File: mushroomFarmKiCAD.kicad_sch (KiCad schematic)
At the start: 10 parts

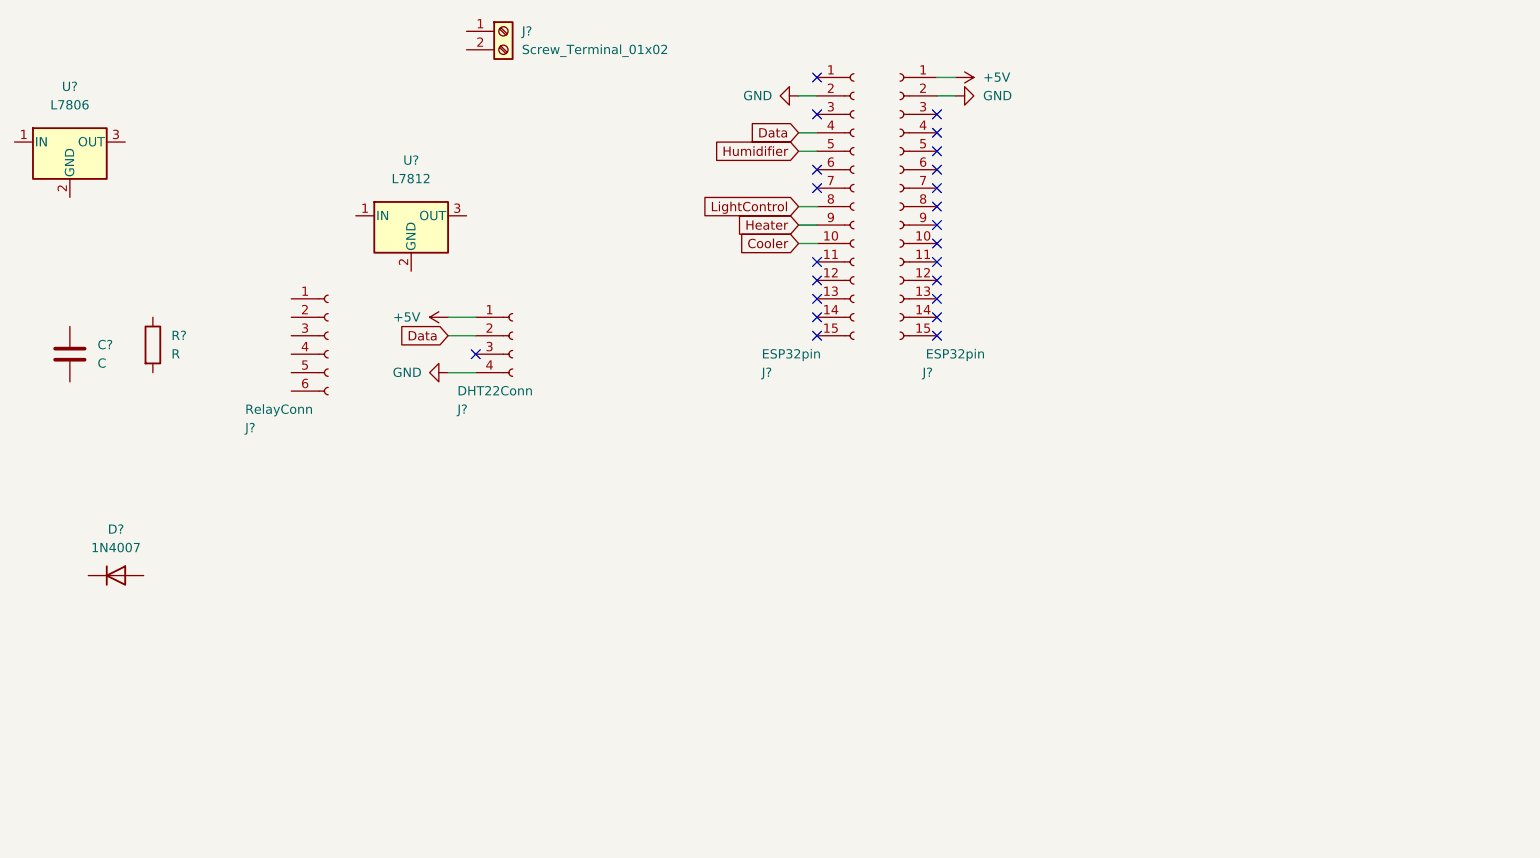
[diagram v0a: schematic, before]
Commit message: design circuit with wire and finalize schematic
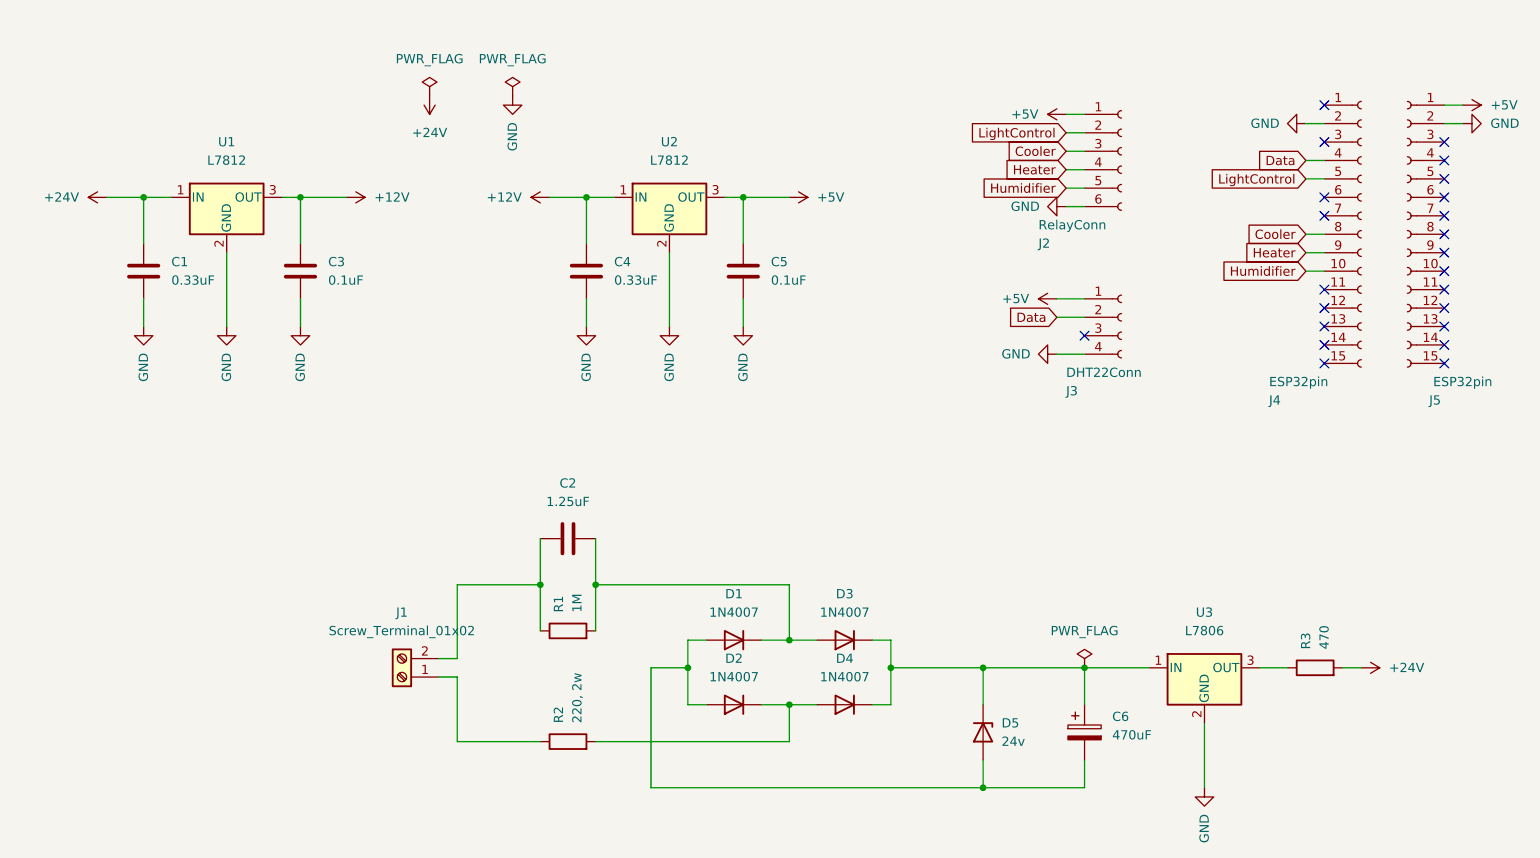
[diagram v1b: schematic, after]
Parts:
- added C2: 1.25uF, Capacitor_THT:C_Disc_D16.0mm_W5.0mm_P10.00mm, symbol Device:C
- added C3, C5: 0.1uF, Capacitor_THT:CP_Radial_D10.0mm_P5.00mm, symbol Device:C
- added C4: 0.33uF, Capacitor_THT:CP_Radial_D10.0mm_P5.00mm, symbol Device:C
- added C6: 470uF, Capacitor_THT:CP_Radial_D10.0mm_P5.00mm, symbol Device:C_Polarized
- added D1, D3, D4: 1N4007, Diode_THT:D_DO-41_SOD81_P10.16mm_Horizontal, symbol Diode:1N4007
- added D5: 24v, Diode_THT:D_DO-41_SOD81_P10.16mm_Horizontal, symbol Device:D_Zener
- added R2: 220, 2w, Resistor_THT:R_Axial_DIN0411_L9.9mm_D3.6mm_P12.70mm_Horizontal, symbol Device:R
- added R3: 470, Resistor_THT:R_Axial_DIN0411_L9.9mm_D3.6mm_P12.70mm_Horizontal, symbol Device:R
- added U2: L7812, Package_TO_SOT_THT:TO-262-3_Vertical, symbol Regulator_Linear:L7812
- C1: renamed from C?; value C -> 0.33uF; footprint (none) -> Capacitor_THT:CP_Radial_D8.0mm_P3.80mm
- J1: renamed from J?; footprint (none) -> TerminalBlock_Altech:Altech_AK300_1x02_P5.00mm_45-Degree
- J2: renamed from J?; footprint (none) -> Connector_PinHeader_2.54mm:PinHeader_1x06_P2.54mm_Vertical
- J3: renamed from J?; footprint (none) -> Connector_PinHeader_2.54mm:PinHeader_1x04_P2.54mm_Vertical
- J4: renamed from J?; footprint Connector_PinHeader_1.00mm:PinHeader_1x15_P1.00mm_Vertical -> Connector_PinHeader_2.54mm:PinHeader_1x15_P2.54mm_Vertical
- J5: renamed from J?; footprint (none) -> Connector_PinHeader_2.54mm:PinHeader_1x15_P2.54mm_Vertical
- R1: renamed from R?; value R -> 1M; footprint (none) -> Resistor_THT:R_Axial_DIN0411_L9.9mm_D3.6mm_P12.70mm_Horizontal
- U1, U3: renamed from U?; footprint (none) -> Package_TO_SOT_THT:TO-262-3_Vertical
- gave numbers to parts that had none: 1
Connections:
- net +5V: now also J2.1 (Pin_1), C5.1, U2.3 (OUT)
- net Cooler: now also J2.3 (Pin_3), J4.8 (Pin_8); no longer J4.10 (Pin_10)
- net GND: now also C1.2, J2.6 (Pin_6), U1.2 (GND), U3.2 (GND), C3.2, C4.2, C5.2, U2.2 (GND)
- net Heater: now also J2.4 (Pin_4)
- net Humidifier: now also J2.5 (Pin_5), J4.10 (Pin_10); no longer J4.5 (Pin_5)
- net LightControl: now also J2.2 (Pin_2), J4.5 (Pin_5); no longer J4.8 (Pin_8)
- net at J1.1 (Pin_1): now also R2.1
- net at J1.2 (Pin_2): now also R1.1, C2.1
- net at D2.1 (K): now also D4.2 (A), R2.2
- net at D2.2 (A): now also C6.2, D1.2 (A), D5.2 (A)
- net at U3.1 (IN): now also C6.1, D3.1 (K), D4.1 (K), D5.1 (K)
- net at U3.3 (OUT): now also R3.1
- net +24V: now reaches C1.1
- net +24V: now also U1.1 (IN), R3.2
- net +12V: now reaches U1.3 (OUT)
- net +12V: now also C3.1, C4.1, U2.1 (IN)
- net at R1.2: now also C2.2, D1.1 (K), D3.2 (A)
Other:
- moved on the sheet: C1, D2, J1, J2, J3, J4, J5, R1, U1, U3

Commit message: Created PCB added 3d models, improve pcb
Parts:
- J1: footprint TerminalBlock_Altech:Altech_AK300_1x02_P5.00mm_45-Degree -> TerminalBlock_Phoenix:TerminalBlock_Phoenix_MKDS-1,5-2_1x02_P5.00mm_Horizontal
- J2: footprint Connector_PinHeader_2.54mm:PinHeader_1x06_P2.54mm_Vertical -> Connector_PinSocket_2.54mm:PinSocket_1x06_P2.54mm_Vertical
- J3: footprint Connector_PinHeader_2.54mm:PinHeader_1x04_P2.54mm_Vertical -> Connector_PinSocket_2.54mm:PinSocket_1x04_P2.54mm_Vertical
- J4, J5: footprint Connector_PinHeader_2.54mm:PinHeader_1x15_P2.54mm_Vertical -> Connector_PinSocket_2.54mm:PinSocket_1x15_P2.54mm_Vertical
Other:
- company: (none) -> Purbanchal University
- title: (none) -> IOT-ENABLED MUSHROOM FARM MONITORING
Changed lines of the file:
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@@
 (kicad_sch (version 20211123) (generator eeschema)
   (paper "A4")
+  (title_block
+    (title "IOT-ENABLED MUSHROOM FARM MONITORING")
+    (date "2022-12-14")
+    (company "Purbanchal University")
+    (comment 1 "Khwopa Engineering College")
+  )
   (junction (at 124.46 124.46) (diameter 0) (color 0 0 0 0)
   )
@@
     (property "Reference" "J1" (id 0) (at 85.09 116.84 0))
     (property "Value" "Screw_Terminal_01x02" (id 1) (at 85.09 119.38 0))
-    (property "Footprint" "TerminalBlock_Altech:Altech_AK300_1x02_P5.00mm_45-Degree" (id 2) (at 85.09 125.73 0)
+    (property "Footprint" "TerminalBlock_Phoenix:TerminalBlock_Phoenix_MKDS-1,5-2_1x02_P5.00mm_Horizontal" (id 2) (at 85.09 125.73 0)
       (effects (font (size 1.27 1.27)) hide)
     )
@@
       (effects (font (size 1.27 1.27)) (justify left))
     )
-    (property "Footprint" "Connector_PinHeader_2.54mm:PinHeader_1x15_P2.54mm_Vertical" (id 2) (at 217.17 64.77 0)
+    (property "Footprint" "Connector_PinSocket_2.54mm:PinSocket_1x15_P2.54mm_Vertical" (id 2) (at 217.17 64.77 0)
       (effects (font (size 1.27 1.27)) hide)
     )
@@
     (property "Reference" "J5" (id 0) (at 227.33 87.63 0))
     (property "Value" "ESP32pin" (id 1) (at 231.14 85.09 0))
-    (property "Footprint" "Connector_PinHeader_2.54mm:PinHeader_1x15_P2.54mm_Vertical" (id 2) (at 223.52 64.77 0)
+    (property "Footprint" "Connector_PinSocket_2.54mm:PinSocket_1x15_P2.54mm_Vertical" (id 2) (at 223.52 64.77 0)
       (effects (font (size 1.27 1.27)) hide)
     )
@@
       (effects (font (size 1.27 1.27)) (justify left))
     )
-    (property "Footprint" "Connector_PinHeader_2.54mm:PinHeader_1x06_P2.54mm_Vertical" (id 2) (at 184.15 53.34 0)
+    (property "Footprint" "Connector_PinSocket_2.54mm:PinSocket_1x06_P2.54mm_Vertical" (id 2) (at 184.15 53.34 0)
       (effects (font (size 1.27 1.27)) hide)
     )
@@
       (effects (font (size 1.27 1.27)) (justify left))
     )
-    (property "Footprint" "Connector_PinHeader_2.54mm:PinHeader_1x04_P2.54mm_Vertical" (id 2) (at 184.15 76.2 0)
+    (property "Footprint" "Connector_PinSocket_2.54mm:PinSocket_1x04_P2.54mm_Vertical" (id 2) (at 184.15 76.2 0)
       (effects (font (size 1.27 1.27)) hide)
     )
@@
     )
     (path "/030d53bf-9274-4b6c-9566-bd9dbac89df1"
-      (reference "J1") (unit 1) (value "Screw_Terminal_01x02") (footprint "TerminalBlock_Altech:Altech_AK300_1x02_P5.00mm_45-Degree")
+      (reference "J1") (unit 1) (value "Screw_Terminal_01x02") (footprint "TerminalBlock_Phoenix:TerminalBlock_Phoenix_MKDS-1,5-2_1x02_P5.00mm_Horizontal")
     )
     (path "/cbf23082-9e00-4345-98bf-ed3e39f1d9fc"
-      (reference "J2") (unit 1) (value "RelayConn") (footprint "Connector_PinHeader_2.54mm:PinHeader_1x06_P2.54mm_Vertical")
+      (reference "J2") (unit 1) (value "RelayConn") (footprint "Connector_PinSocket_2.54mm:PinSocket_1x06_P2.54mm_Vertical")
     )
     (path "/ec4e7991-8d83-483f-86eb-aae2671efd44"
-      (reference "J3") (unit 1) (value "DHT22Conn") (footprint "Connector_PinHeader_2.54mm:PinHeader_1x04_P2.54mm_Vertical")
+      (reference "J3") (unit 1) (value "DHT22Conn") (footprint "Connector_PinSocket_2.54mm:PinSocket_1x04_P2.54mm_Vertical")
     )
     (path "/14a7a41a-7b62-4b9d-8496-102da86f2afa"
-      (reference "J4") (unit 1) (value "ESP32pin") (footprint "Connector_PinHeader_2.54mm:PinHeader_1x15_P2.54mm_Vertical")
+      (reference "J4") (unit 1) (value "ESP32pin") (footprint "Connector_PinSocket_2.54mm:PinSocket_1x15_P2.54mm_Vertical")
     )
     (path "/b1bc582b-832f-438c-b5b7-59e1c8fda712"
-      (reference "J5") (unit 1) (value "ESP32pin") (footprint "Connector_PinHeader_2.54mm:PinHeader_1x15_P2.54mm_Vertical")
+      (reference "J5") (unit 1) (value "ESP32pin") (footprint "Connector_PinSocket_2.54mm:PinSocket_1x15_P2.54mm_Vertical")
     )
     (path "/e3ec2f86-c8f8-4bbf-b210-b2dc15e5917f"
